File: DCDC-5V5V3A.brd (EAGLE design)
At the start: 40 x 24 mm, 31 parts, among them U1 TPS63020DSJR

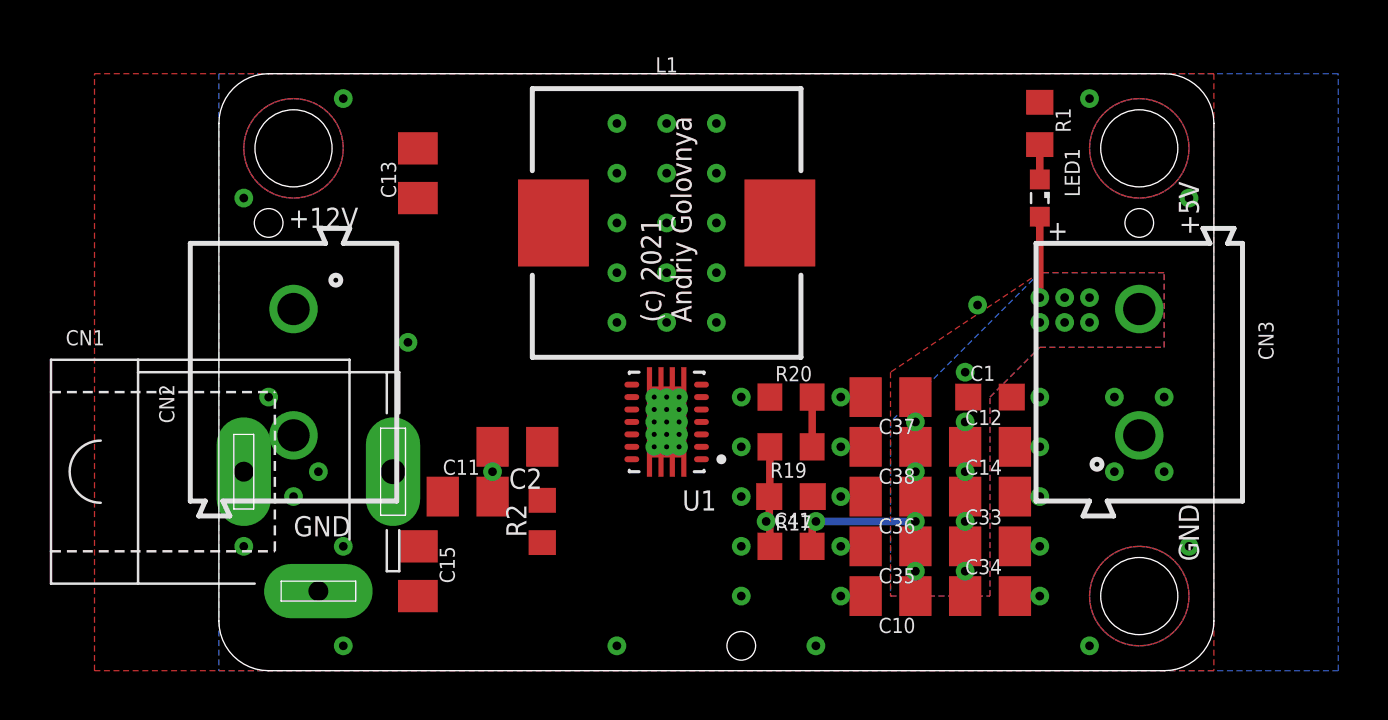
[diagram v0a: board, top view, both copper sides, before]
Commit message: Improved schematics and routing of 5V-5V board. Generated PDF schematics. Generated PNG preview. Generated CAM files.
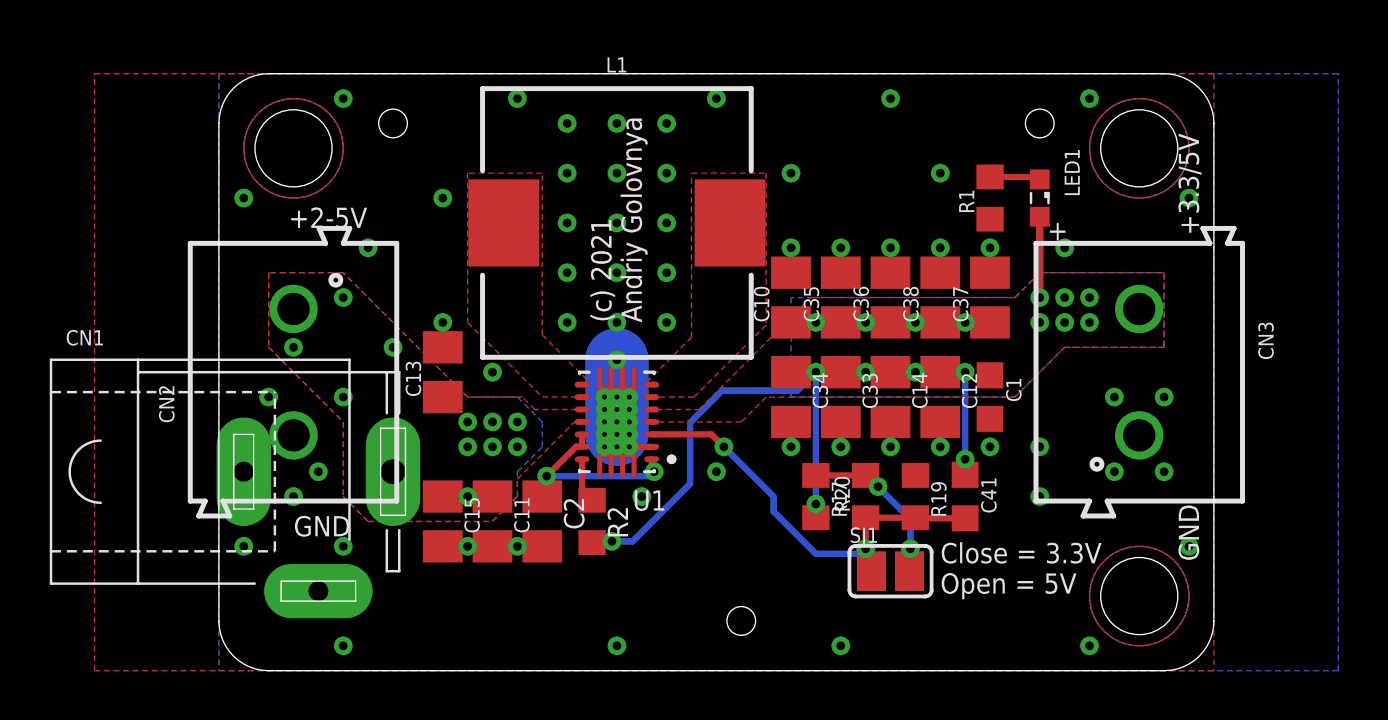
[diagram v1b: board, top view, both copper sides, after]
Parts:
- added SJ1: (no value), _my_jumpers:SJ
- R1: value 2k -> 1k
- R17: value 75k -> 1M
- R19: value 100 -> 180k
- R20: value 10k -> 620k
- moved C10 12.6 mm to (23.0, 15.0), turned to 90 degrees
- moved C34 11.3 mm to (23.0, 11.0), turned to 270 degrees
- moved C35 10.2 mm to (25.0, 15.0), turned to 90 degrees
- moved C33 8.49 mm to (25.0, 11.0), turned to 270 degrees
- moved C13 8.06 mm to (9.00, 12.0)
- moved C36 8.00 mm to (27.0, 15.0), turned to 90 degrees
- moved C41 7.00 mm to (30.0, 7.00), turned to 270 degrees
- moved HOLE2 6.40 mm to (7.00, 22.0)
- moved C38 6.32 mm to (29.0, 15.0), turned to 90 degrees
- moved C14 5.66 mm to (27.0, 11.0), turned to 270 degrees
- moved C37 5.66 mm to (31.0, 15.0), turned to 90 degrees
- moved HOLE1 5.66 mm to (33.0, 22.0)
- moved R19 5.39 mm to (28.0, 7.00), turned to 270 degrees
- moved R20 5.00 mm to (26.0, 7.00), turned to 90 degrees
- moved R1 3.61 mm to (31.0, 19.0), turned to 90 degrees
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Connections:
- net N$3 renamed L1
- net N$4 renamed PG
- net N$5 renamed L2
- net N$7 renamed VINA
- net FB: now also R20.1, SJ1.1; no longer R17.1
- net GND: now also R19.1; no longer R20.1
- net N$2: now also R17.1, SJ1.2; no longer R19.1
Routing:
- net VOUT: track 8.49 -> 26.5 mm, vias 16 -> 17
- net FB: track 4.12 -> 17.3 mm, vias 1 -> 2
- net VINA: track 0.00 -> 8.28 mm, vias 0 -> 2
- net GND: track 0.00 -> 5.11 mm, vias 51 -> 60
- net N$2: track 2.00 -> 6.64 mm, vias 0 -> 2
- net PG: track 0.00 -> 1.82 mm
- net N$1: track 1.40 -> 2.04 mm
- added copper zone on layer 1, net L1
- added copper zone on layer 1, net L2
- added copper zone on layer 1, net VIN
- added copper zone on layer 16, net VIN
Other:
- board text added: "+3.3/5V"
- board text added: "2-5V/3A Buck-Boost Converter"
- board text added: "Close = 3.3V Open = 5V"
- board text removed: "+12V"
- board text removed: "+5V"
- board text removed: "2-5V/3A DC-DC Buck-Boost Converter"

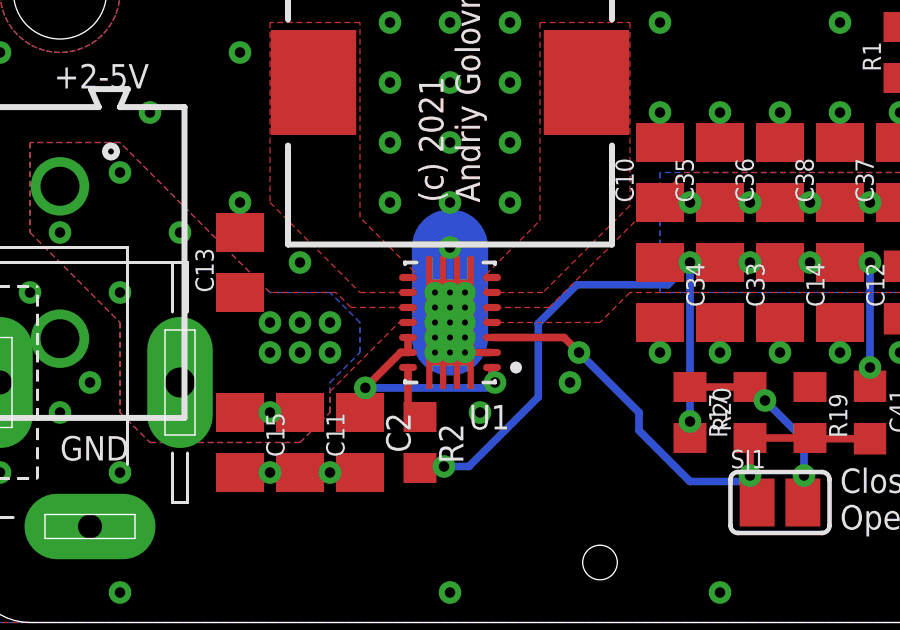
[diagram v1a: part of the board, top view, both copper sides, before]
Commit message: Improved routing of 5V-5V board. Generated PNG preview. Generated CAM files.
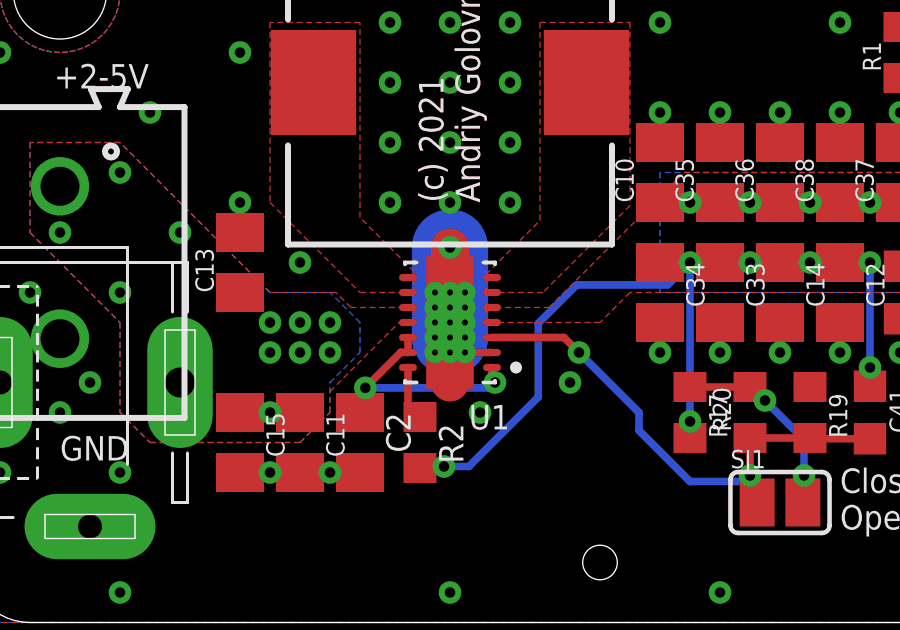
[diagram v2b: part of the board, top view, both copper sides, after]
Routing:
- net GND: track 5.11 -> 9.61 mm
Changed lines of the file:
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@@
 <wire x1="16.5" y1="9" x2="17.4" y2="9" width="0.254" layer="1"/>
 <wire x1="16" y1="12.5" x2="16" y2="9.5" width="2.54" layer="16"/>
+<wire x1="16" y1="12.5" x2="16" y2="8" width="1.27" layer="1"/>
 </signal>
 <signal name="VOUT" airwireshidden="yes">

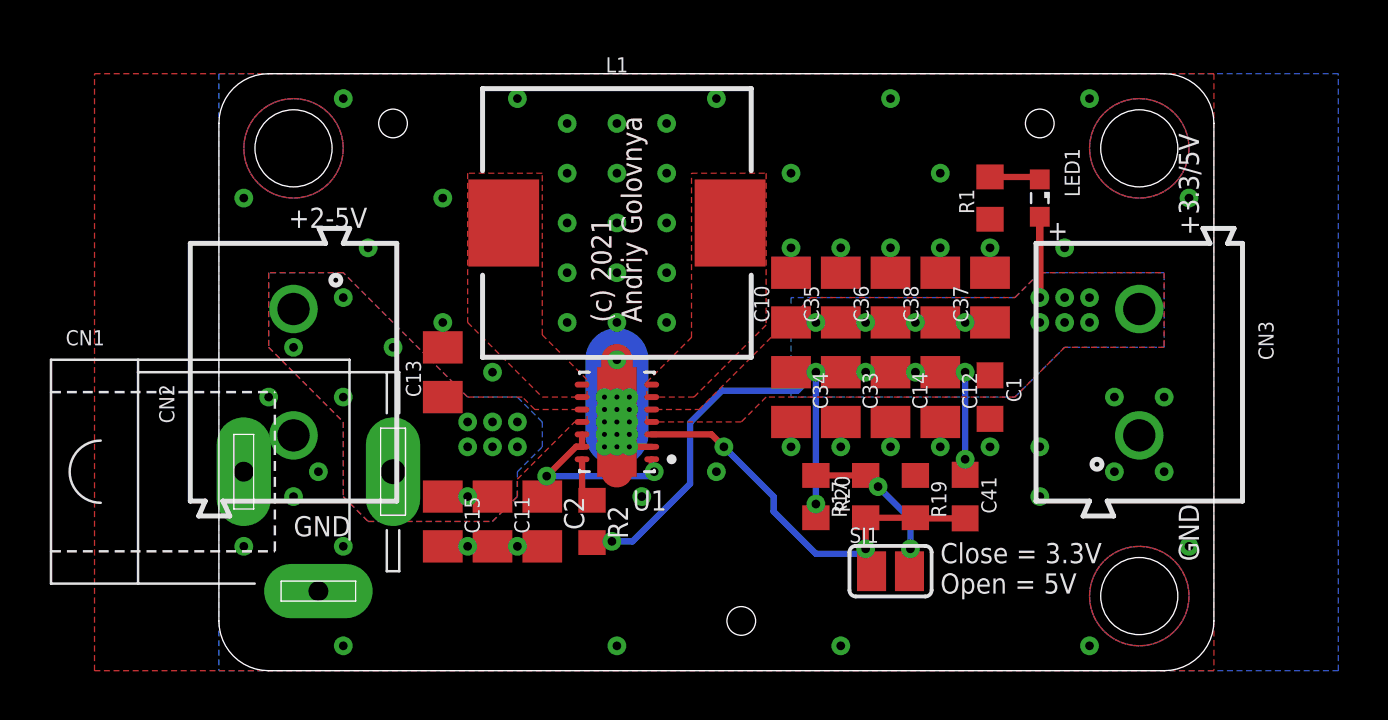
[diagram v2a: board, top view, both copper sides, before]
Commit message: Fixed few traces. Generated CAM files. Generated PNG preview.
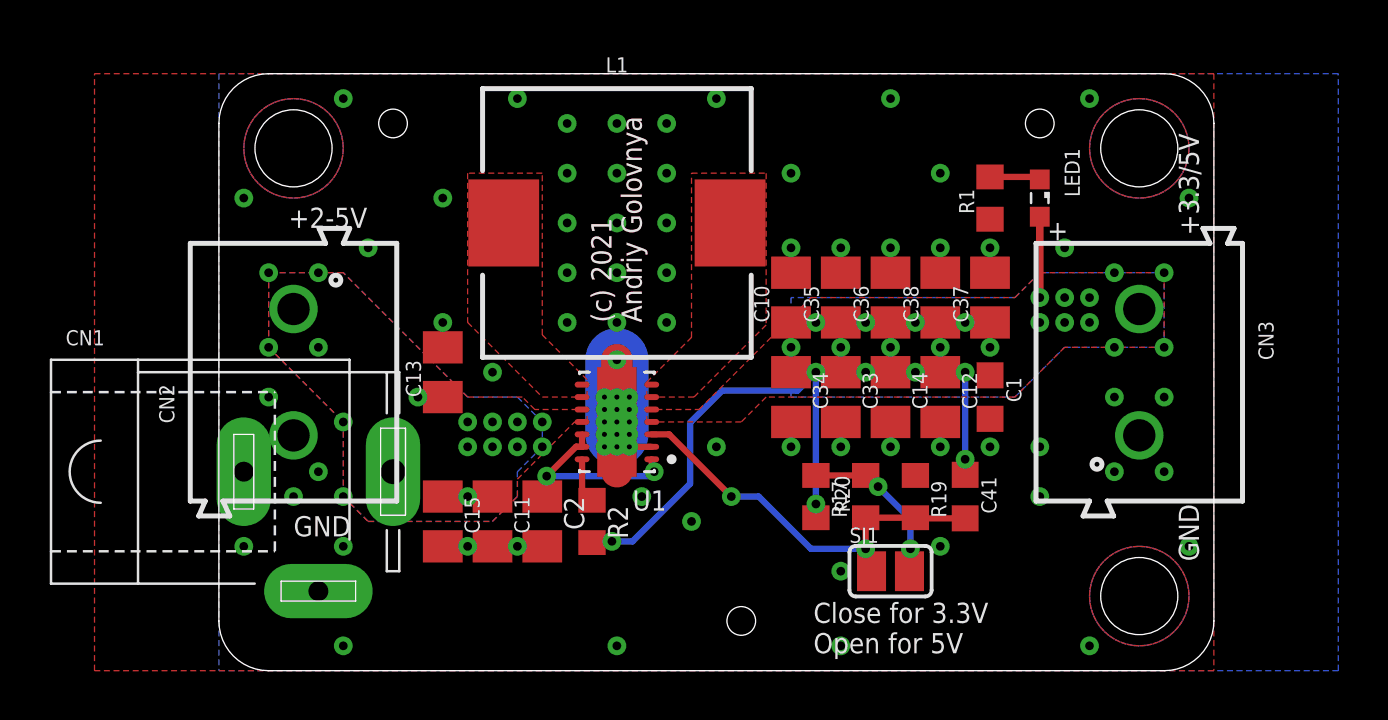
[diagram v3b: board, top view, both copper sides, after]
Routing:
- net FB: track 17.3 -> 16.8 mm
- net VOUT: vias 17 -> 26
- net GND: vias 60 -> 63
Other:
- board text added: "Close for 3.3V Open for 5V"
- board text removed: "Close = 3.3V Open = 5V"
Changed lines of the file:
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@@
 <text x="17" y="14" size="0.8128" layer="21" font="vector" ratio="20" rot="R90">(c) 2021
 Andriy Golovnya</text>
-<text x="29" y="3.1" size="0.8128" layer="21" font="vector">Close = 3.3V
-Open = 5V</text>
+<text x="23.9" y="0.7" size="0.8128" layer="21" font="vector">Close for 3.3V
+Open for 5V</text>
 </plain>
 <attributes>
@@
 <vertex x="5" y="16"/>
 </polygon>
-<via x="5" y="15" extent="1-16" drill="0.35"/>
-<via x="5" y="11" extent="1-16" drill="0.35"/>
-<via x="7" y="13" extent="1-16" drill="0.35"/>
+<via x="4" y="16" extent="1-16" drill="0.35"/>
+<via x="4" y="13" extent="1-16" drill="0.35"/>
+<via x="5" y="10" extent="1-16" drill="0.35"/>
 <via x="12" y="10" extent="1-16" drill="0.35"/>
 <via x="12" y="9" extent="1-16" drill="0.35"/>
@@
 <via x="10" y="9" extent="1-16" drill="0.35"/>
 <via x="10" y="7" extent="1-16" drill="0.35"/>
-<via x="3" y="13" extent="1-16" drill="0.35"/>
+<via x="2" y="13" extent="1-16" drill="0.35"/>
+<via x="13" y="10" extent="1-16" drill="0.35"/>
+<via x="5" y="7" extent="1-16" drill="0.35"/>
+<via x="8" y="11" extent="1-16" drill="0.35"/>
+<via x="13" y="9" extent="1-16" drill="0.35"/>
+<via x="2" y="16" extent="1-16" drill="0.35"/>
 </signal>
 <signal name="GND" airwireshidden="yes">
@@
 <via x="31" y="9" extent="1-16" drill="0.35"/>
 <via x="11" y="12" extent="1-16" drill="0.35"/>
-<via x="20" y="8" extent="1-16" drill="0.35"/>
+<via x="20" y="9" extent="1-16" drill="0.35"/>
 <via x="16" y="12.5" extent="1-16" drill="0.35"/>
 <via x="12" y="23" extent="1-16" drill="0.35"/>
@@
 <wire x1="16" y1="12.5" x2="16" y2="9.5" width="2.54" layer="16"/>
 <wire x1="16" y1="12.5" x2="16" y2="8" width="1.27" layer="1"/>
+<via x="19" y="6" extent="1-16" drill="0.35"/>
+<via x="25" y="4" extent="1-16" drill="0.35"/>
+<via x="29" y="5" extent="1-16" drill="0.35"/>
 </signal>
 <signal name="VOUT" airwireshidden="yes">
@@
 <wire x1="15.8" y1="5.2" x2="15.75" y2="5.15" width="0.254" layer="1"/>
 <wire x1="15.75" y1="5.15" x2="15" y2="5.15" width="0.254" layer="1"/>
+<via x="38" y="16" extent="1-16" drill="0.35"/>
+<via x="38" y="13" extent="1-16" drill="0.35"/>
+<via x="23" y="13" extent="1-16" drill="0.35"/>
+<via x="25" y="13" extent="1-16" drill="0.35"/>
+<via x="27" y="13" extent="1-16" drill="0.35"/>
+<via x="29" y="13" extent="1-16" drill="0.35"/>
+<via x="31" y="13" extent="1-16" drill="0.35"/>
+<via x="36" y="16" extent="1-16" drill="0.35"/>
+<via x="36" y="13" extent="1-16" drill="0.35"/>
 </signal>
 <signal name="FB">
@@
 <wire x1="26" y1="4.9" x2="26" y2="4.238" width="0.254" layer="1"/>
 <wire x1="26" y1="4.238" x2="26.238" y2="4" width="0.254" layer="1"/>
-<wire x1="17.4" y1="9.5" x2="19.8" y2="9.5" width="0.254" layer="1"/>
-<wire x1="19.8" y1="9.5" x2="20.3" y2="9" width="0.254" layer="1"/>
-<via x="20.3" y="9" extent="1-16" drill="0.35"/>
-<wire x1="24" y1="4.7" x2="22.3" y2="6.4" width="0.254" layer="16"/>
-<wire x1="20.3" y1="9" x2="22.3" y2="7" width="0.254" layer="16"/>
-<wire x1="22.3" y1="7" x2="22.3" y2="6.4" width="0.254" layer="16"/>
-<wire x1="25.8" y1="4.7" x2="26" y2="4.9" width="0.254" layer="16"/>
-<wire x1="25.8" y1="4.7" x2="24" y2="4.7" width="0.254" layer="16"/>
+<wire x1="17.4" y1="9.5" x2="18.1" y2="9.5" width="0.254" layer="1"/>
+<wire x1="18.1" y1="9.5" x2="20.6" y2="7" width="0.254" layer="1"/>
+<via x="20.6" y="7" extent="1-16" drill="0.35"/>
+<wire x1="23.8" y1="4.9" x2="21.7" y2="7" width="0.254" layer="16"/>
+<wire x1="20.6" y1="7" x2="21.7" y2="7" width="0.254" layer="16"/>
+<wire x1="26" y1="4.9" x2="23.8" y2="4.9" width="0.254" layer="16"/>
 <via x="26" y="4.9" extent="1-16" drill="0.35"/>
 </signal>

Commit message: Moved some texts and tooling holes a bit. Generated CAM files. Generated PNG preview. Generated PDF schematics. Renamed BoM and PnP files.
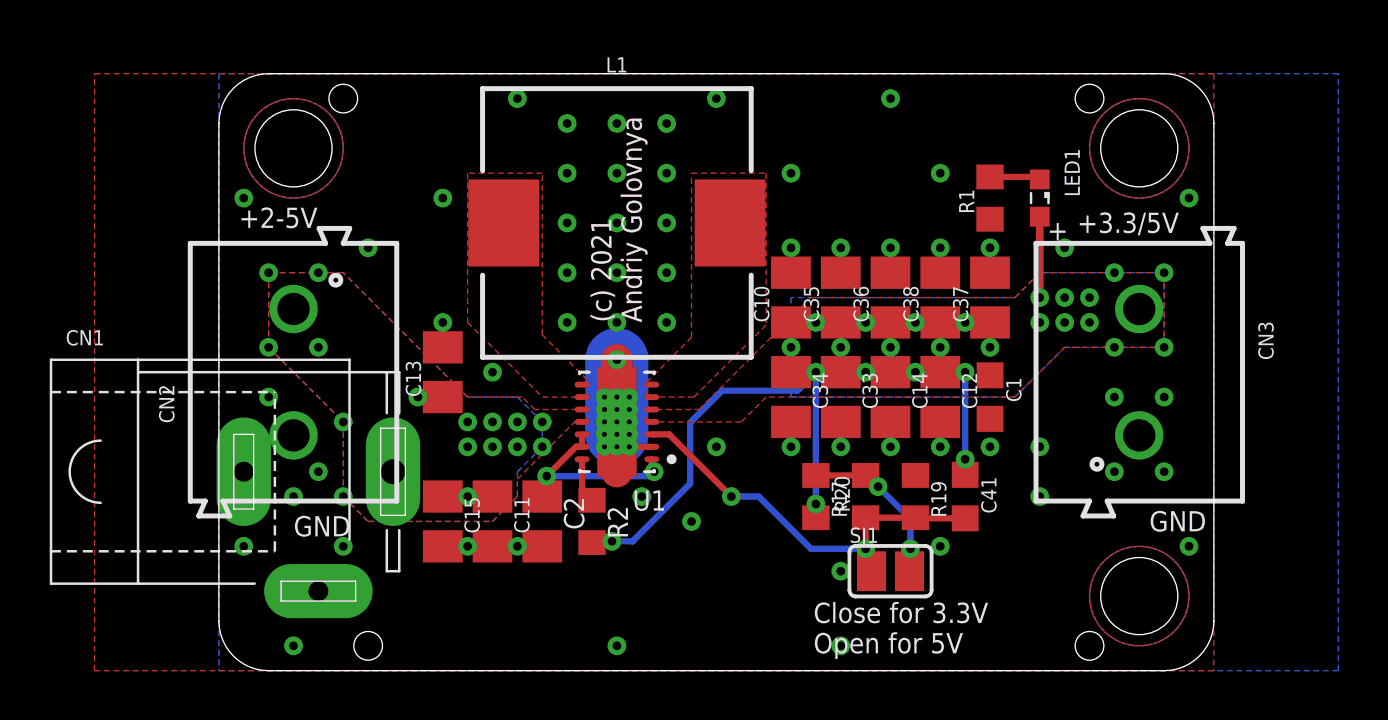
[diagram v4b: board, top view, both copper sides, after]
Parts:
- added HOLE4: TOOLINGHOLE, _my_fiducia:TOOLING-HOLE
- moved HOLE3 14.0 mm to (35.0, 1.00)
- moved HOLE1 2.24 mm to (35.0, 23.0)
- moved HOLE2 2.24 mm to (5.00, 23.0)
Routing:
- net GND: vias 63 -> 60
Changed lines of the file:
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@@
 <hole x="37" y="3" drill="3.1"/>
 <text x="33" y="20" size="1.6764" layer="22" font="vector" ratio="20" rot="MR0">DCDC-5V5V3A-0010</text>
-<text x="2.8" y="17.8" size="0.8128" layer="21" font="vector">+2-5V</text>
+<text x="0.8" y="17.8" size="0.8128" layer="21" font="vector">+2-5V</text>
 <text x="3" y="5.4" size="0.8128" layer="21" font="vector">GND</text>
-<text x="39.4" y="4.4" size="0.8128" layer="21" font="vector" rot="R90">GND</text>
-<text x="39.4" y="17.5" size="0.8128" layer="21" font="vector" rot="R90">+3.3/5V</text>
+<text x="37.4" y="5.6" size="0.8128" layer="21" font="vector">GND</text>
+<text x="34.5" y="17.6" size="0.8128" layer="21" font="vector">+3.3/5V</text>
 <text x="33" y="16" size="1.27" layer="22" font="vector" rot="MR0">(c) Andriy Golovnya</text>
 <text x="33" y="18" size="1.27" layer="22" font="vector" rot="MR0">2-5V/3A Buck-Boost Converter</text>
@@
 <attribute name="VALUE" x="32.905" y="18.365" size="0.6096" layer="27" font="vector" rot="R90"/>
 </element>
-<element name="HOLE1" library="_my_fiducia" package="TOOLING-HOLE" value="TOOLINGHOLE" x="33" y="22" smashed="yes"/>
-<element name="HOLE2" library="_my_fiducia" package="TOOLING-HOLE" value="TOOLINGHOLE" x="7" y="22" smashed="yes"/>
-<element name="HOLE3" library="_my_fiducia" package="TOOLING-HOLE" value="TOOLINGHOLE" x="21" y="2" smashed="yes"/>
+<element name="HOLE1" library="_my_fiducia" package="TOOLING-HOLE" value="TOOLINGHOLE" x="35" y="23" smashed="yes"/>
+<element name="HOLE2" library="_my_fiducia" package="TOOLING-HOLE" value="TOOLINGHOLE" x="5" y="23" smashed="yes"/>
+<element name="HOLE3" library="_my_fiducia" package="TOOLING-HOLE" value="TOOLINGHOLE" x="35" y="1" smashed="yes"/>
 <element name="C1" library="rcl" library_urn="urn:adsk.eagle:library:334" package="C0603K" package3d_urn="urn:adsk.eagle:package:23680/2" value="1nF" x="31" y="11" smashed="yes" rot="R270">
 <attribute name="NAME" x="31.65" y="11.8" size="0.6096" layer="25" font="vector" rot="R270"/>
@@
 <attribute name="VALUE" x="27.4001" y="4" size="0.02" layer="27"/>
 </element>
+<element name="HOLE4" library="_my_fiducia" package="TOOLING-HOLE" value="TOOLINGHOLE" x="6" y="1" smashed="yes"/>
 </elements>
 <signals>
@@
 <via x="33" y="9" extent="1-16" drill="0.35"/>
 <via x="33" y="7" extent="1-16" drill="0.35"/>
-<via x="5" y="23" extent="1-16" drill="0.35"/>
-<via x="35" y="23" extent="1-16" drill="0.35"/>
 <via x="39" y="19" extent="1-16" drill="0.35"/>
 <via x="39" y="5" extent="1-16" drill="0.35"/>
@@
 <via x="1" y="5" extent="1-16" drill="0.35"/>
 <via x="1" y="19" extent="1-16" drill="0.35"/>
-<via x="35" y="1" extent="1-16" drill="0.35"/>
 <via x="38" y="11" extent="1-16" drill="0.35"/>
 <via x="36" y="11" extent="1-16" drill="0.35"/>
@@
 <via x="4" y="8" extent="1-16" drill="0.35"/>
 <via x="2" y="11" extent="1-16" drill="0.35"/>
-<via x="5" y="1" extent="1-16" drill="0.35"/>
+<via x="3" y="1" extent="1-16" drill="0.35"/>
 <via x="12" y="5" extent="1-16" drill="0.35"/>
 <via x="25" y="1" extent="1-16" drill="0.35"/>
